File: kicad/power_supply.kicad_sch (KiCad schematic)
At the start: 63 parts, among them J2 Cliff DC10A, Q1 2N2905A, Q2 2N2905A, Q3 2N3904, Q4 2N3904, U11 7406, U16 MC34063AP, U18 LM7805, U19 LM317T, U20 LM317T

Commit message: KiCAD: Customize IC footprint silk screen
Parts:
- U11: footprint Package_DIP:DIP-14_W7.62mm_Socket -> custom_footprints:DIP-14_W7.62mm_Socket
- U16: footprint Package_DIP:DIP-8_W7.62mm_Socket -> custom_footprints:DIP-8_W7.62mm_Socket
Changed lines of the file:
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@@
     (property "Reference" "U11" (id 0) (at 129.54 93.345 0))
     (property "Value" "7406" (id 1) (at 129.54 90.805 0))
-    (property "Footprint" "Package_DIP:DIP-14_W7.62mm_Socket" (id 2) (at 129.54 86.36 0)
+    (property "Footprint" "custom_footprints:DIP-14_W7.62mm_Socket" (id 2) (at 129.54 86.36 0)
       (effects (font (size 1.27 1.27)) hide)
     )
@@
     (property "Reference" "U11" (id 0) (at 179.07 157.48 0))
     (property "Value" "7406" (id 1) (at 179.07 154.94 0))
-    (property "Footprint" "Package_DIP:DIP-14_W7.62mm_Socket" (id 2) (at 179.07 149.86 0)
+    (property "Footprint" "custom_footprints:DIP-14_W7.62mm_Socket" (id 2) (at 179.07 149.86 0)
       (effects (font (size 1.27 1.27)) hide)
     )
@@
     (property "Reference" "U11" (id 0) (at 242.57 157.48 0))
     (property "Value" "7406" (id 1) (at 242.57 154.94 0))
-    (property "Footprint" "Package_DIP:DIP-14_W7.62mm_Socket" (id 2) (at 242.57 149.86 0)
+    (property "Footprint" "custom_footprints:DIP-14_W7.62mm_Socket" (id 2) (at 242.57 149.86 0)
       (effects (font (size 1.27 1.27)) hide)
     )
@@
     (property "Reference" "U11" (id 0) (at 172.72 93.98 0))
     (property "Value" "7406" (id 1) (at 172.72 91.44 0))
-    (property "Footprint" "Package_DIP:DIP-14_W7.62mm_Socket" (id 2) (at 172.72 86.36 0)
+    (property "Footprint" "custom_footprints:DIP-14_W7.62mm_Socket" (id 2) (at 172.72 86.36 0)
       (effects (font (size 1.27 1.27)) hide)
     )
@@
     (property "Reference" "U16" (id 0) (at 69.85 33.02 0))
     (property "Value" "MC34063AP" (id 1) (at 69.85 35.56 0))
-    (property "Footprint" "Package_DIP:DIP-8_W7.62mm_Socket" (id 2) (at 71.12 57.15 0)
+    (property "Footprint" "custom_footprints:DIP-8_W7.62mm_Socket" (id 2) (at 71.12 57.15 0)
       (effects (font (size 1.27 1.27)) (justify left) hide)
     )
@@
     (property "Reference" "U11" (id 0) (at 161.29 166.37 0))
     (property "Value" "7406" (id 1) (at 161.29 168.91 0))
-    (property "Footprint" "Package_DIP:DIP-14_W7.62mm_Socket" (id 2) (at 161.29 175.26 0)
+    (property "Footprint" "custom_footprints:DIP-14_W7.62mm_Socket" (id 2) (at 161.29 175.26 0)
       (effects (font (size 1.27 1.27)) hide)
     )
@@
       (effects (font (size 1.27 1.27)) (justify left))
     )
-    (property "Footprint" "Package_DIP:DIP-14_W7.62mm_Socket" (id 2) (at 129.54 173.99 0)
+    (property "Footprint" "custom_footprints:DIP-14_W7.62mm_Socket" (id 2) (at 129.54 173.99 0)
       (effects (font (size 1.27 1.27)) hide)
     )
@@
     (property "Reference" "U11" (id 0) (at 129.54 106.045 0))
     (property "Value" "7406" (id 1) (at 129.54 103.505 0))
-    (property "Footprint" "Package_DIP:DIP-14_W7.62mm_Socket" (id 2) (at 129.54 98.425 0)
-      (effects (font (size 1.27 1.27)) hide)
-    )
+    (property "Footprint" "custom_footprints:DIP-14_W7.62mm_Socket" (id 2) (at 129.54 98.425 0)
+      (effects (font (size 1.27 1.27)) hide)
+    )

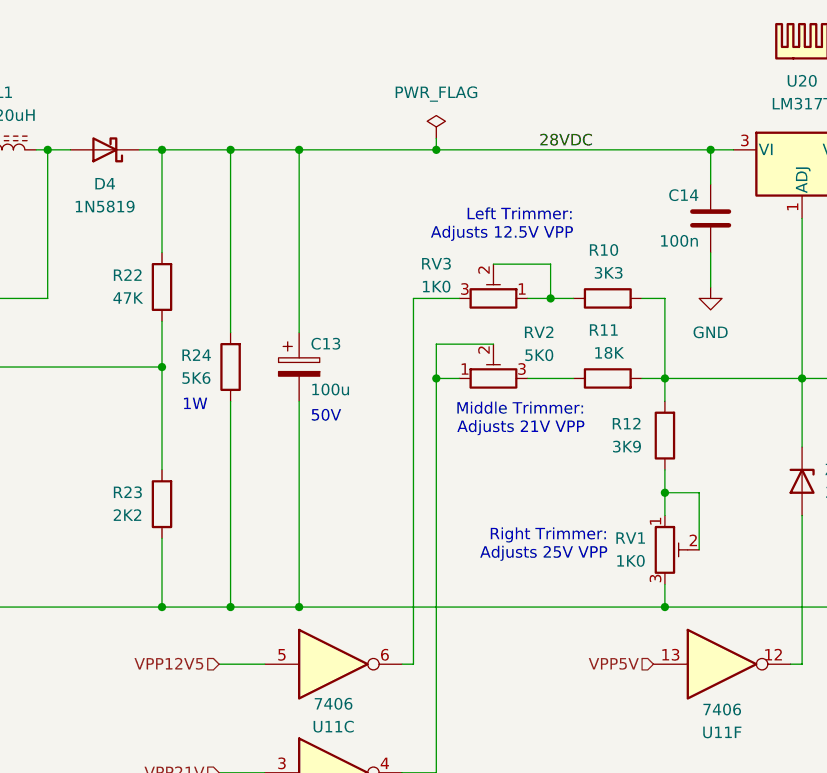
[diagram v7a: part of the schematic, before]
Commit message: KiCAD: larger footprint for 1W resistors
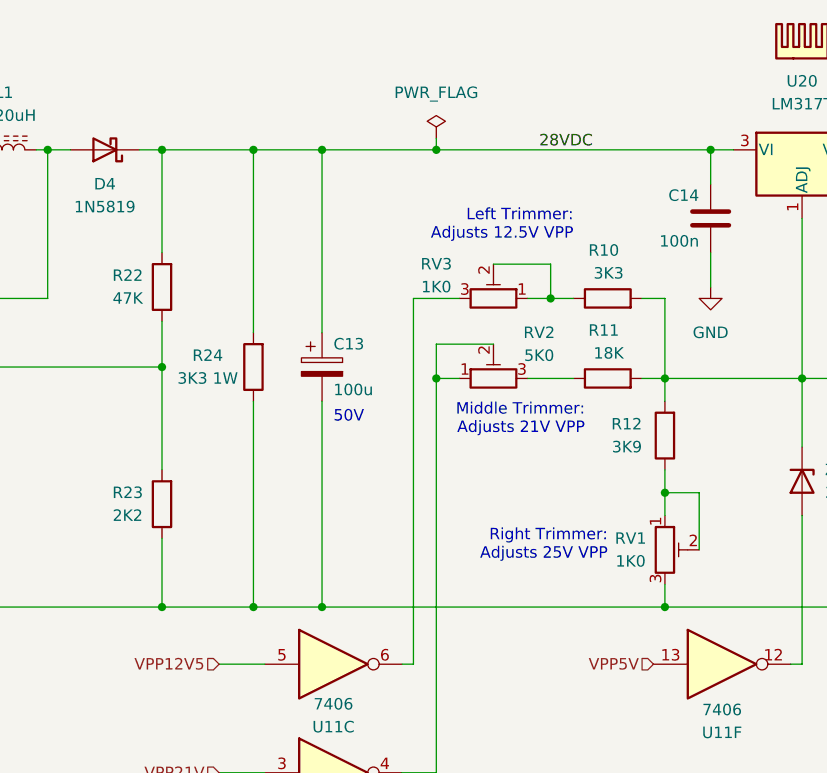
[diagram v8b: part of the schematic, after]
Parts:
- R24: value 5K6 -> 3K3 1W; footprint Resistor_THT:R_Axial_DIN0207_L6.3mm_D2.5mm_P10.16mm_Horizontal -> Resistor_THT:R_Axial_DIN0309_L9.0mm_D3.2mm_P12.70mm_Horizontal
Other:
- note removed: "1W"
- moved on the sheet: C13, R24
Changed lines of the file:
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@@
   (junction (at 198.12 143.51) (diameter 0) (color 0 0 0 0)
   )
-  (junction (at 118.11 29.21) (diameter 0) (color 0 0 0 0)
-  )
   (junction (at 110.49 80.01) (diameter 0) (color 0 0 0 0)
   )
@@
   (junction (at 48.26 40.64) (diameter 0) (color 0 0 0 0)
   )
+  (junction (at 128.27 29.21) (diameter 0) (color 0 0 0 0)
+  )
   (junction (at 232.41 127) (diameter 0) (color 0 0 0 0)
   )
@@
   (junction (at 119.38 143.51) (diameter 0) (color 0 0 0 0)
   )
-  (junction (at 125.73 29.21) (diameter 0) (color 0 0 0 0)
-  )
   (junction (at 171.45 29.21) (diameter 0) (color 0 0 0 0)
   )
   (junction (at 68.58 127) (diameter 0) (color 0 0 0 0)
   )
-  (junction (at 118.11 80.01) (diameter 0) (color 0 0 0 0)
-  )
   (junction (at 246.38 80.01) (diameter 0) (color 0 0 0 0)
   )
@@
   (junction (at 45.72 114.3) (diameter 0) (color 0 0 0 0)
   )
-  (junction (at 125.73 80.01) (diameter 0) (color 0 0 0 0)
-  )
   (junction (at 254 114.3) (diameter 0) (color 0 0 0 0)
   )
+  (junction (at 120.65 80.01) (diameter 0) (color 0 0 0 0)
+  )
   (junction (at 45.72 143.51) (diameter 0) (color 0 0 0 0)
   )
@@
   (junction (at 57.15 80.01) (diameter 0) (color 0 0 0 0)
   )
+  (junction (at 120.65 29.21) (diameter 0) (color 0 0 0 0)
+  )
   (junction (at 208.28 114.3) (diameter 0) (color 0 0 0 0)
   )
@@
   )
   (junction (at 203.2 80.01) (diameter 0) (color 0 0 0 0)
+  )
+  (junction (at 128.27 80.01) (diameter 0) (color 0 0 0 0)
   )
   (junction (at 78.74 127) (diameter 0) (color 0 0 0 0)
@@
     (stroke (width 0) (type default) (color 0 0 0 0))
   )
-  (wire (pts (xy 118.11 80.01) (xy 125.73 80.01))
-    (stroke (width 0) (type default) (color 0 0 0 0))
-  )
   (wire (pts (xy 242.57 114.3) (xy 254 114.3))
     (stroke (width 0) (type default) (color 0 0 0 0))
@@
     (stroke (width 0) (type default) (color 0 0 0 0))
   )
-  (wire (pts (xy 110.49 29.21) (xy 118.11 29.21))
-    (stroke (width 0) (type default) (color 0 0 0 0))
-  )
   (wire (pts (xy 224.79 29.21) (xy 224.79 39.37))
     (stroke (width 0) (type default) (color 0 0 0 0))
   )
-  (wire (pts (xy 110.49 80.01) (xy 118.11 80.01))
-    (stroke (width 0) (type default) (color 0 0 0 0))
-  )
   (wire (pts (xy 198.12 143.51) (xy 208.28 143.51))
     (stroke (width 0) (type default) (color 0 0 0 0))
@@
     (stroke (width 0) (type default) (color 0 0 0 0))
   )
+  (wire (pts (xy 120.65 29.21) (xy 128.27 29.21))
+    (stroke (width 0) (type default) (color 0 0 0 0))
+  )
   (wire (pts (xy 45.72 80.01) (xy 45.72 81.28))
     (stroke (width 0) (type default) (color 0 0 0 0))
@@
     (stroke (width 0) (type default) (color 0 0 0 0))
   )
+  (wire (pts (xy 110.49 80.01) (xy 120.65 80.01))
+    (stroke (width 0) (type default) (color 0 0 0 0))
+  )
   (wire (pts (xy 163.83 54.61) (xy 166.37 54.61))
     (stroke (width 0) (type default) (color 0 0 0 0))
@@
     (stroke (width 0) (type default) (color 0 0 0 0))
   )
-  (wire (pts (xy 125.73 57.15) (xy 125.73 80.01))
+  (wire (pts (xy 128.27 57.15) (xy 128.27 80.01))
     (stroke (width 0) (type default) (color 0 0 0 0))
   )
@@
     (stroke (width 0) (type default) (color 0 0 0 0))
   )
-  (wire (pts (xy 118.11 29.21) (xy 118.11 49.53))
+  (wire (pts (xy 120.65 29.21) (xy 120.65 49.53))
     (stroke (width 0) (type default) (color 0 0 0 0))
   )
@@
     (stroke (width 0) (type default) (color 0 0 0 0))
   )
-  (wire (pts (xy 118.11 57.15) (xy 118.11 80.01))
+  (wire (pts (xy 120.65 57.15) (xy 120.65 80.01))
     (stroke (width 0) (type default) (color 0 0 0 0))
   )
@@
     (stroke (width 0) (type default) (color 0 0 0 0))
   )
-  (wire (pts (xy 118.11 29.21) (xy 125.73 29.21))
+  (wire (pts (xy 110.49 29.21) (xy 120.65 29.21))
     (stroke (width 0) (type default) (color 0 0 0 0))
   )
@@
     (stroke (width 0) (type default) (color 0 0 0 0))
   )
-  (wire (pts (xy 125.73 29.21) (xy 125.73 49.53))
+  (wire (pts (xy 128.27 29.21) (xy 128.27 49.53))
     (stroke (width 0) (type default) (color 0 0 0 0))
   )
@@
     (stroke (width 0) (type default) (color 0 0 0 0))
   )
-  (wire (pts (xy 125.73 80.01) (xy 166.37 80.01))
-    (stroke (width 0) (type default) (color 0 0 0 0))
-  )
   (wire (pts (xy 237.49 114.3) (xy 242.57 114.3))
     (stroke (width 0) (type default) (color 0 0 0 0))
@@
     (stroke (width 0) (type default) (color 0 0 0 0))
   )
+  (wire (pts (xy 128.27 29.21) (xy 140.97 29.21))
+    (stroke (width 0) (type default) (color 0 0 0 0))
+  )
   (wire (pts (xy 88.9 127) (xy 99.06 127))
     (stroke (width 0) (type default) (color 0 0 0 0))
@@
     (stroke (width 0) (type default) (color 0 0 0 0))
   )
+  (wire (pts (xy 128.27 80.01) (xy 166.37 80.01))
+    (stroke (width 0) (type default) (color 0 0 0 0))
+  )
   (wire (pts (xy 99.06 127) (xy 99.06 130.81))
     (stroke (width 0) (type default) (color 0 0 0 0))
@@
     (stroke (width 0) (type default) (color 0 0 0 0))
   )
-  (wire (pts (xy 125.73 29.21) (xy 140.97 29.21))
-    (stroke (width 0) (type default) (color 0 0 0 0))
-  )
   (wire (pts (xy 96.52 29.21) (xy 97.79 29.21))
+    (stroke (width 0) (type default) (color 0 0 0 0))
+  )
+  (wire (pts (xy 120.65 80.01) (xy 128.27 80.01))
     (stroke (width 0) (type default) (color 0 0 0 0))
   )
@@
     (effects (font (size 1.27 1.27)) (justify left bottom))
   )
-  (text "1W" (at 115.57 58.42 180)
-    (effects (font (size 1.27 1.27)) (justify right bottom))
-  )
   (text "Left Trimmer:\nAdjusts 12.5V VPP" (at 156.21 39.37 180)
     (effects (font (size 1.27 1.27)) (justify right bottom))
@@
     (effects (font (size 1.27 1.27)) (justify left bottom))
   )
-  (text "50V" (at 127 59.69 0)
+  (text "50V" (at 129.54 59.69 0)
     (effects (font (size 1.27 1.27)) (justify left bottom))
   )
@@
     (pin "2")
   )
-  (symbol (lib_id "Device:R") (at 118.11 53.34 180) (unit 1)
-    (in_bom yes) (on_board yes)
-    (property "Reference" "R24" (id 0) (at 114.3 52.07 0))
-    (property "Value" "5K6" (id 1) (at 114.3 54.61 0))
-    (property "Footprint" "Resistor_THT:R_Axial_DIN0207_L6.3mm_D2.5mm_P10.16mm_Horizontal" (id 2) (at 119.888 53.34 90)
-      (effects (font (size 1.27 1.27)) hide)
-    )
-    (property "Datasheet" "~" (id 3) (at 118.11 53.34 0)
+  (symbol (lib_id "Device:R") (at 120.65 53.34 180) (unit 1)
+    (in_bom yes) (on_board yes)
+    (property "Reference" "R24" (id 0) (at 115.57 52.07 0))
+    (property "Value" "3K3 1W" (id 1) (at 115.57 54.61 0))
+    (property "Footprint" "Resistor_THT:R_Axial_DIN0309_L9.0mm_D3.2mm_P12.70mm_Horizontal" (id 2) (at 122.428 53.34 90)
+      (effects (font (size 1.27 1.27)) hide)
+    )
+    (property "Datasheet" "~" (id 3) (at 120.65 53.34 0)
       (effects (font (size 1.27 1.27)) hide)
     )
@@
     (pin "3")
   )
-  (symbol (lib_id "Device:C_Polarized") (at 125.73 53.34 0) (unit 1)
-    (in_bom yes) (on_board yes)
-    (property "Reference" "C13" (id 0) (at 127 50.8 0)
-      (effects (font (size 1.27 1.27)) (justify left))
-    )
-    (property "Value" "100u" (id 1) (at 127 55.88 0)
-      (effects (font (size 1.27 1.27)) (justify left))
-    )
-    (property "Footprint" "Capacitor_THT:CP_Radial_D8.0mm_P5.00mm" (id 2) (at 126.6952 57.15 0)
-      (effects (font (size 1.27 1.27)) hide)
-    )
-    (property "Datasheet" "~" (id 3) (at 125.73 53.34 0)
-      (effects (font (size 1.27 1.27)) hide)
-    )
+  (symbol (lib_id "Device:C_Polarized") (at 128.27 53.34 0) (unit 1)
+    (in_bom yes) (on_board yes)
+    (property "Reference" "C13" (id 0) (at 129.54 50.8 0)
+      (effects (font (size 1.27 1.27)) (justify left))
+    )
+    (property "Value" "100u" (id 1) (at 129.54 55.88 0)
+      (effects (font (size 1.27 1.27)) (justify left))
+    )
+    (property "Footprint" "Capacitor_THT:CP_Radial_D8.0mm_P5.00mm" (id 2) (at 129.2352 57.15 0)
+      (effects (font (size 1.27 1.27)) hide)
+    )
+    (property "Datasheet" "~" (id 3) (at 128.27 53.34 0)
+      (effects (font (size 1.27 1.27)) hide)
+    )
